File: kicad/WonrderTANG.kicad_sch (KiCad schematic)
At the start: 31 parts, among them CON1 MSX-CONNECTOR, J1 Conn_02x01, J2 AudioJack3, J3 Conn_02x01, Q1 2N3904, U1 SN74LVC245AN, U2 SN74LVC245AN, U3 SN74LVC245AN, U4 SN74LVC245AN, U5 Tang_Nano_20k, U6 SN74LVC245AN

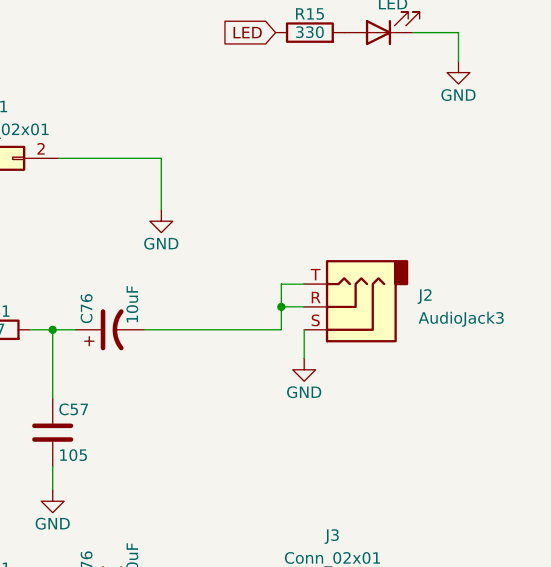
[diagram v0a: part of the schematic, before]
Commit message: [kicad] Use alternate audio connector SJ1-3525N
Exchange the SJ1-3533NG mono audio connector with the more common
(at least in Europe and some large asian shops) SJ1-3525N stereo
connector, keeping the same orientation.
To fit the new connector the board led is slightly moved too.
This modification also allows to keep the audio connector within
the standard cartridge case depth.

Signed-off-by: Albert Herranz <albert_herranz@yahoo.es>
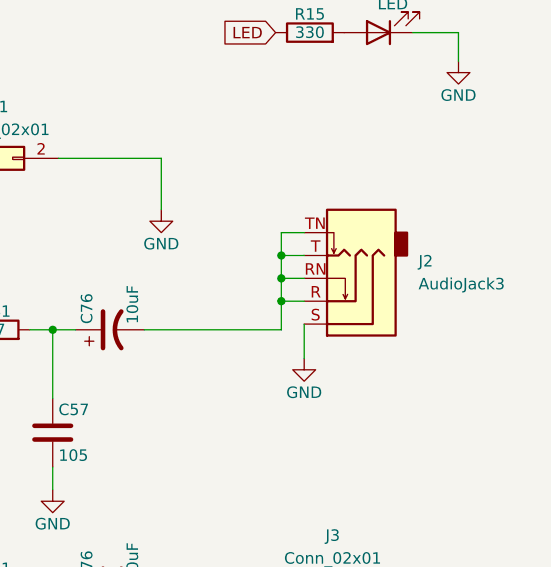
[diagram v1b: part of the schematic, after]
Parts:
- J2: footprint Connector_Audio:Jack_3.5mm_CUI_SJ1-3533NG_Horizontal -> Connector_Audio:Jack_3.5mm_CUI_SJ1-3525N_Horizontal; symbol Connector_Audio:AudioJack3 -> Connector_Audio:AudioJack3_SwitchTR
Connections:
- net at C76.2, J2.R, J2.T: now also J2.RN, J2.TN
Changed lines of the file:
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@@
     (date "2023-03-01")
   )
+  (junction (at 363.22 106.68) (diameter 0) (color 0 0 0 0)
+  )
   (junction (at 101.6 147.32) (diameter 0) (color 0 0 0 0)
   )
@@
   (junction (at 101.6 154.94) (diameter 0) (color 0 0 0 0)
   )
-  (junction (at 363.22 107.315) (diameter 0) (color 0 0 0 0)
+  (junction (at 363.22 104.14) (diameter 0) (color 0 0 0 0)
   )
   (junction (at 337.82 138.43) (diameter 0) (color 0 0 0 0)
   )
   (junction (at 337.82 109.855) (diameter 0) (color 0 0 0 0)
+  )
+  (junction (at 363.22 101.6) (diameter 0) (color 0 0 0 0)
   )
   (no_connect (at 325.12 55.88))
@@
     (stroke (width 0) (type default))
   )
-  (wire (pts (xy 365.76 109.855) (xy 365.76 113.03))
+  (wire (pts (xy 365.76 109.22) (xy 365.76 113.03))
     (stroke (width 0) (type default))
   )
@@
     (stroke (width 0) (type default))
   )
+  (wire (pts (xy 363.22 106.68) (xy 363.22 109.855))
+    (stroke (width 0) (type default))
+  )
   (wire (pts (xy 113.03 182.88) (xy 113.03 184.15))
     (stroke (width 0) (type default))
@@
     (stroke (width 0) (type default))
   )
-  (wire (pts (xy 363.22 104.775) (xy 363.22 107.315))
+  (wire (pts (xy 363.22 104.14) (xy 363.22 106.68))
     (stroke (width 0) (type default))
   )
@@
     (stroke (width 0) (type default))
   )
-  (wire (pts (xy 363.22 107.315) (xy 365.76 107.315))
+  (wire (pts (xy 363.22 106.68) (xy 365.76 106.68))
     (stroke (width 0) (type default))
   )
@@
     (stroke (width 0) (type default))
   )
+  (wire (pts (xy 365.76 99.06) (xy 363.22 99.06))
+    (stroke (width 0) (type default))
+  )
   (wire (pts (xy 295.91 58.42) (xy 299.72 58.42))
     (stroke (width 0) (type default))
@@
     (stroke (width 0) (type default))
   )
+  (wire (pts (xy 365.76 101.6) (xy 363.22 101.6))
+    (stroke (width 0) (type default))
+  )
   (wire (pts (xy 201.93 55.88) (xy 204.47 55.88))
     (stroke (width 0) (type default))
@@
     (stroke (width 0) (type default))
   )
+  (wire (pts (xy 363.22 99.06) (xy 363.22 101.6))
+    (stroke (width 0) (type default))
+  )
   (wire (pts (xy 201.93 107.95) (xy 204.47 107.95))
     (stroke (width 0) (type default))
@@
     (stroke (width 0) (type default))
   )
-  (wire (pts (xy 365.76 104.775) (xy 363.22 104.775))
+  (wire (pts (xy 365.76 104.14) (xy 363.22 104.14))
     (stroke (width 0) (type default))
   )
@@
     (stroke (width 0) (type default))
   )
-  (wire (pts (xy 363.22 109.855) (xy 363.22 107.315))
-    (stroke (width 0) (type default))
-  )
   (wire (pts (xy 149.86 139.7) (xy 152.4 139.7))
     (stroke (width 0) (type default))
@@
   )
   (wire (pts (xy 149.86 144.78) (xy 152.4 144.78))
+    (stroke (width 0) (type default))
+  )
+  (wire (pts (xy 363.22 101.6) (xy 363.22 104.14))
     (stroke (width 0) (type default))
   )
@@
     )
   )
-  (symbol (lib_id "Connector_Audio:AudioJack3") (at 370.84 107.315 180) (unit 1)
+  (symbol (lib_id "Connector_Audio:AudioJack3_SwitchTR") (at 370.84 106.68 180) (unit 1)
     (in_bom yes) (on_board yes) (dnp no) (fields_autoplaced)
-    (property "Reference" "J2" (at 378.46 106.045 0)
+    (property "Reference" "J2" (at 378.46 102.235 0)
       (effects (font (size 1.27 1.27)) (justify right))
     )
-    (property "Value" "AudioJack3" (at 378.46 108.585 0)
+    (property "Value" "AudioJack3" (at 378.46 104.775 0)
       (effects (font (size 1.27 1.27)) (justify right))
     )
-    (property "Footprint" "Connector_Audio:Jack_3.5mm_CUI_SJ1-3533NG_Horizontal" (at 370.84 107.315 0)
-      (effects (font (size 1.27 1.27)) hide)
-    )
-    (property "Datasheet" "~" (at 370.84 107.315 0)
+    (property "Footprint" "Connector_Audio:Jack_3.5mm_CUI_SJ1-3525N_Horizontal" (at 370.84 106.68 0)
+      (effects (font (size 1.27 1.27)) hide)
+    )
+    (property "Datasheet" "~" (at 370.84 106.68 0)
       (effects (font (size 1.27 1.27)) hide)
     )
@@
     (pin "S")
     (pin "T")
+    (pin "TN")
+    (pin "RN")
     (instances
       (project "WonrderTANG"
